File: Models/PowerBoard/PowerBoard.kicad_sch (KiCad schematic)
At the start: 0 parts

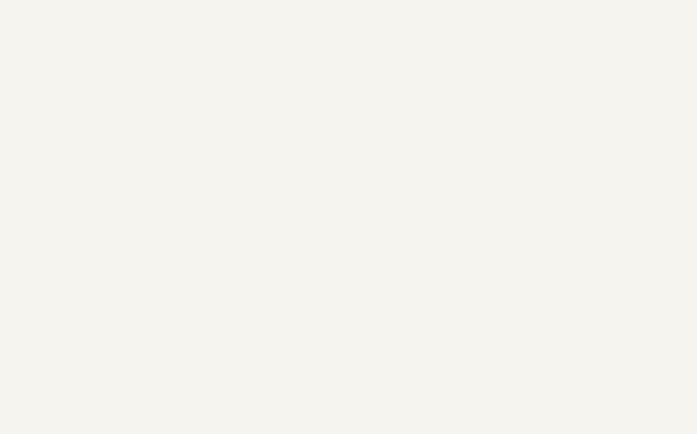
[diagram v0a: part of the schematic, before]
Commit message: Added mounting holes
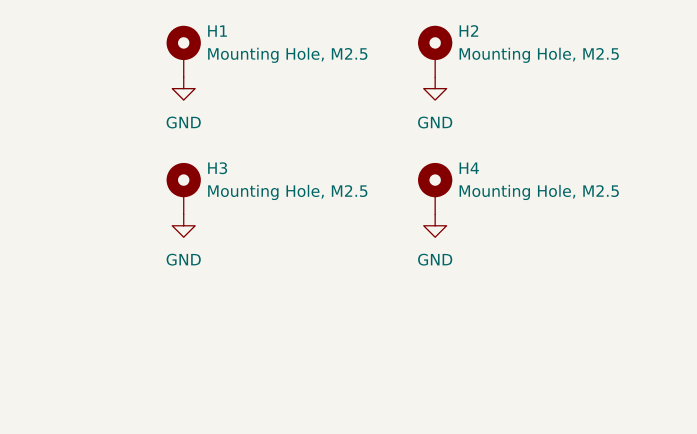
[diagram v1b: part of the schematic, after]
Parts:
- added H1, H2, H3, H4: Mounting Hole, M2.5, MountingHole:MountingHole_2.7mm_M2.5_DIN965_Pad, symbol Mechanical:MountingHole_Pad
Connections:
- new net GND: H1.1, H2.1, H3.1, H4.1

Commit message: Save progress
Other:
- note added: "15V: shielded -15V: shielded"
- note added: "18V: no external interface -18V: no external interface"
- note added: "5V (preamp): breadboard -5V (preamp): breadboard 2.5V: shielded -1.5V: shielded"
- note added: "5V: no external interface 3.3V: no external interface"
- note added: "interface to main board: many pin/socket connections external interface (shielded): (1) SMA (2) 1x4 pin socket, GND + OUT + OUT + GND external interface (breadboard): (1) 1x4 pin socket, GND + OUT + OUT + GND"
- note removed: "Allocate 2 pins on a large pin socket for each of the following nodes, in case design revisions require more boards: - 18V - -18V - GND - 5V (converter) - 3.3V - GND - 5V (preamp) - -5V (preamp)"

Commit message: Save progress
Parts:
- added J11, J14, J15, J5, J7, J9: Conn_01x04_Socket, symbol Connector:Conn_01x04_Socket
- added J12, J13, J4, J6: Conn_Coaxial, symbol Connector:Conn_Coaxial
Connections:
- net GND: now also J11.1 (Pin_1), J11.4 (Pin_4), J12.2 (Ext), J13.2 (Ext), J14.1 (Pin_1), J14.4 (Pin_4), J15.1 (Pin_1), J15.4 (Pin_4), J4.2 (Ext), J5.1 (Pin_1), J5.4 (Pin_4), J6.2 (Ext), J7.1 (Pin_1), J7.4 (Pin_4), J9.1 (Pin_1), J9.4 (Pin_4)
- new net: J14.2 (Pin_2), J14.3 (Pin_3)
- new net: J5.2 (Pin_2), J5.3 (Pin_3)
- new net: J11.2 (Pin_2), J11.3 (Pin_3)
- new net: J9.2 (Pin_2), J9.3 (Pin_3)
- new net: J7.2 (Pin_2), J7.3 (Pin_3)
- new net: J15.2 (Pin_2), J15.3 (Pin_3)
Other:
- moved on the sheet: H1, H2, H3, H4

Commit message: Save progress
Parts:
- added J8: Conn_01x09_Socket, symbol Connector:Conn_01x09_Socket
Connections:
- net -1.5V: now also J13.1 (In), J15.2 (Pin_2), J15.3 (Pin_3)
- net -15V: now also J6.1 (In), J7.2 (Pin_2), J7.3 (Pin_3), J8.4 (Pin_4)
- net 15V: now also J4.1 (In), J5.2 (Pin_2), J5.3 (Pin_3), J8.2 (Pin_2)
- net 2.5V: now also J12.1 (In), J14.2 (Pin_2), J14.3 (Pin_3)
- net 3.3V: now also J8.8 (Pin_8)
- net 5V: now also J8.6 (Pin_6)
- net GND: now also J8.1 (Pin_1), J8.3 (Pin_3), J8.5 (Pin_5), J8.7 (Pin_7), J8.9 (Pin_9)
- net -5V_PreAmp: now reaches J11.2 (Pin_2), J11.3 (Pin_3)
- net 5V_PreAmp: now reaches J9.2 (Pin_2), J9.3 (Pin_3)
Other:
- moved on the sheet: H1, H2, H3, H4

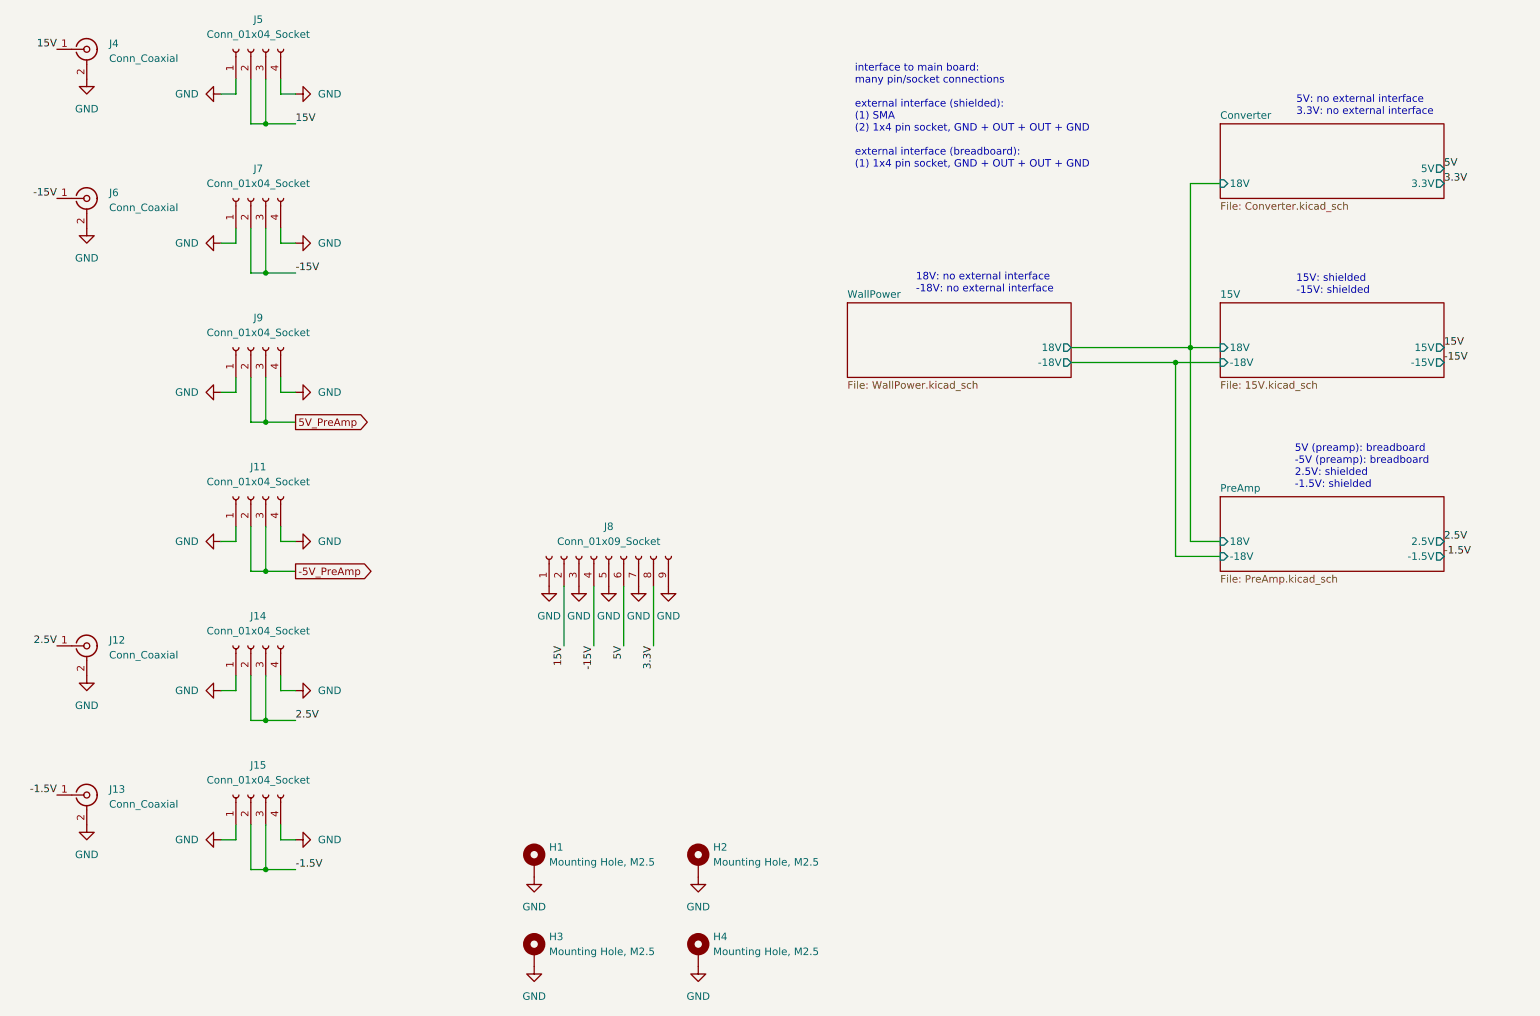
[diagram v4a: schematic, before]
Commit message: Connectors should be fully specified now
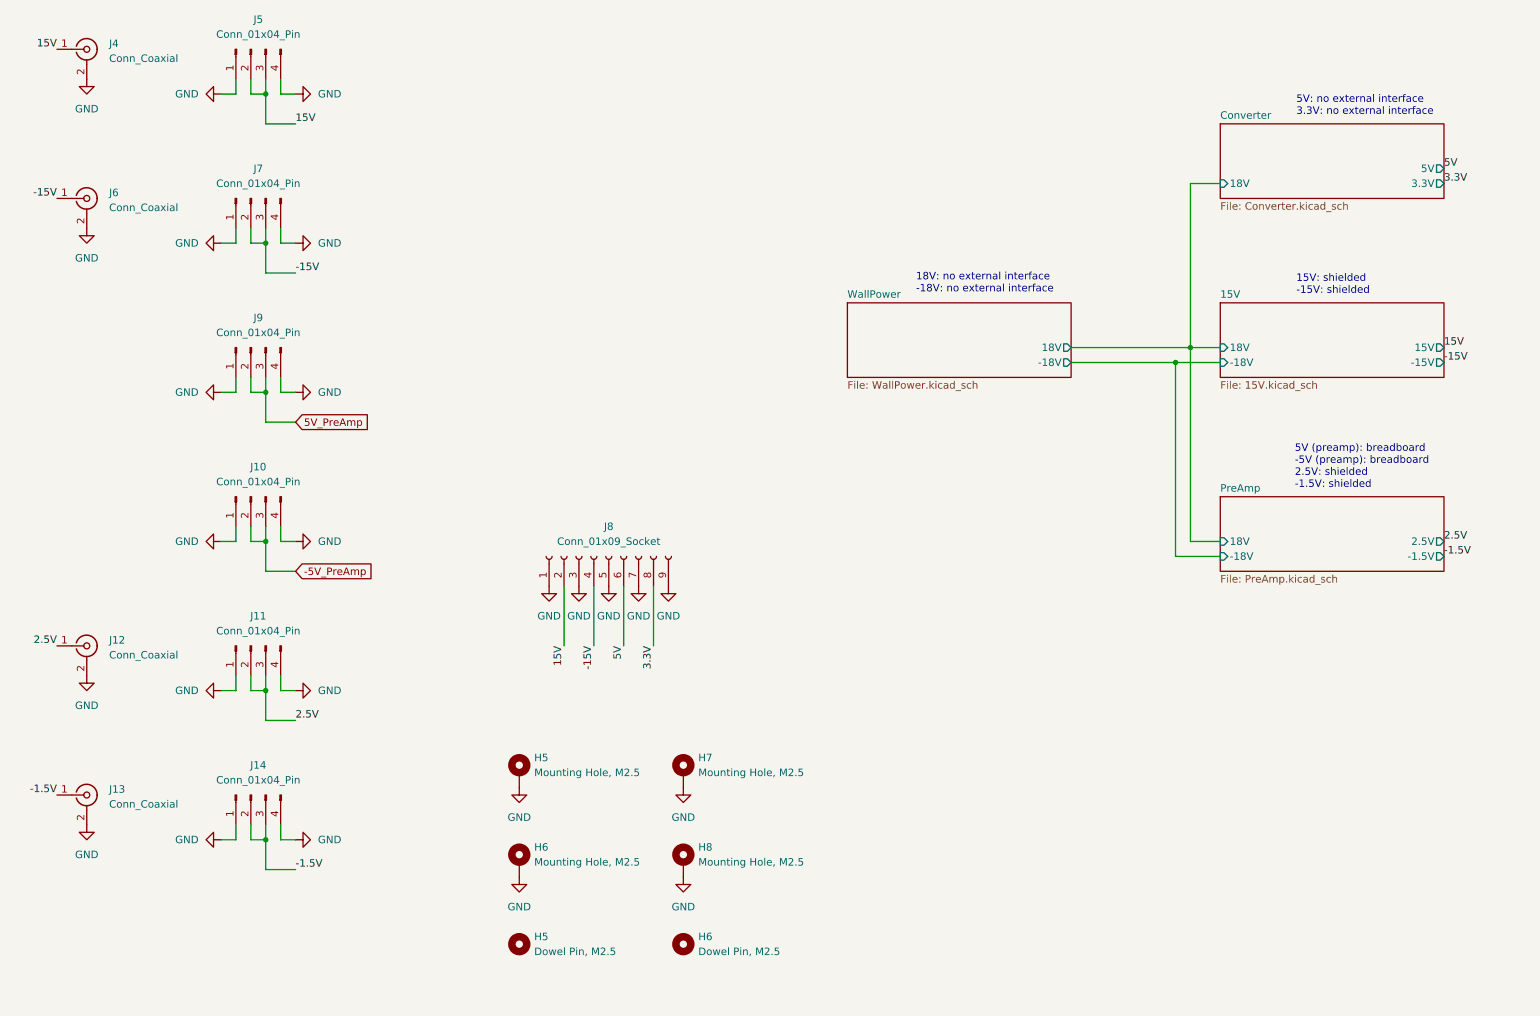
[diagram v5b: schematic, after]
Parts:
- removed H1, H2, H3, H4: Mounting Hole, M2.5, MountingHole:MountingHole_2.7mm_M2.5_DIN965_Pad, symbol Mechanical:MountingHole_Pad
- removed J11, J14, J15, J5, J7, J9: Conn_01x04_Socket, symbol Connector:Conn_01x04_Socket
- added H5, H6: Dowel Pin, M2.5, symbol Mechanical:MountingHole
- added H5, H6, H7, H8: Mounting Hole, M2.5, MountingHole:MountingHole_2.7mm_M2.5_DIN965_Pad, symbol Mechanical:MountingHole_Pad
- added J10, J11, J14, J5, J7, J9: Conn_01x04_Pin, symbol Connector:Conn_01x04_Pin
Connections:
- net -1.5V: now also J14.2 (Pin_2), J14.3 (Pin_3)
- net -15V: now also J7.2 (Pin_2), J7.3 (Pin_3)
- net -5V_PreAmp: now also J10.2 (Pin_2), J10.3 (Pin_3)
- net 15V: now also J5.2 (Pin_2), J5.3 (Pin_3)
- net 2.5V: now also J11.2 (Pin_2), J11.3 (Pin_3)
- net 5V_PreAmp: now also J9.2 (Pin_2), J9.3 (Pin_3)
- net GND: now also H5.1, H6.1, H7.1, H8.1, J10.1 (Pin_1), J10.4 (Pin_4), J11.1 (Pin_1), J11.4 (Pin_4), J14.1 (Pin_1), J14.4 (Pin_4), J5.1 (Pin_1), J5.4 (Pin_4), J7.1 (Pin_1), J7.4 (Pin_4), J9.1 (Pin_1), J9.4 (Pin_4)
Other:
- note removed: "interface to main board: many pin/socket connections external interface (shielded): (1) SMA (2) 1x4 pin socket, GND + OUT + OUT + GND external interface (breadboard): (1) 1x4 pin socket, GND + OUT + OUT + GND"

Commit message: Passes ERC
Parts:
- renumbered H5 to H1, H6 to H2, H5 to H3, H7 to H4, H8 to H5, J4 to J1, J14 to J10, J8 to J11, J6 to J2, J12 to J3, J13 to J4, J7 to J6, J9 to J7, J10 to J8, J11 to J9

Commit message: Assigned footprints
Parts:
- H1, H2, H4, H5: footprint MountingHole:MountingHole_2.7mm_M2.5_DIN965_Pad -> Connector_Custom:Keystone_24929
- H3, H6: footprint (none) -> Connector_Custom:DowelPin_2.5mm
- J1, J2, J3, J4: footprint (none) -> Connector_Custom:RFPC-SMA27-F
- J10, J5, J6, J7, J8, J9: footprint (none) -> Connector_Custom:PinConnector_1x4
- J11: footprint (none) -> Connector_Custom:PinConnector_1x9
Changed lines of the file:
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@@
 			)
 		)
-		(property "Footprint" ""
+		(property "Footprint" "Connector_Custom:RFPC-SMA27-F"
 			(at 38.1 50.8 0)
 			(effects
@@
 			)
 		)
-		(property "Footprint" ""
+		(property "Footprint" "Connector_Custom:DowelPin_2.5mm"
 			(at 139.7 177.8 0)
 			(effects
@@
 			)
 		)
-		(property "Footprint" ""
+		(property "Footprint" "Connector_Custom:PinConnector_1x4"
 			(at 66.04 152.4 0)
 			(effects
@@
 			)
 		)
-		(property "Footprint" ""
+		(property "Footprint" "Connector_Custom:DowelPin_2.5mm"
 			(at 111.76 177.8 0)
 			(effects
@@
 			)
 		)
-		(property "Footprint" ""
+		(property "Footprint" "Connector_Custom:RFPC-SMA27-F"
 			(at 38.1 127 0)
 			(effects
@@
 			)
 		)
-		(property "Footprint" "MountingHole:MountingHole_2.7mm_M2.5_DIN965_Pad"
+		(property "Footprint" "Connector_Custom:Keystone_24929"
 			(at 139.7 163.83 0)
 			(effects
@@
 			)
 		)
-		(property "Footprint" ""
+		(property "Footprint" "Connector_Custom:PinConnector_1x9"
 			(at 127 111.76 0)
 			(effects
@@
 			)
 		)
-		(property "Footprint" "MountingHole:MountingHole_2.7mm_M2.5_DIN965_Pad"
+		(property "Footprint" "Connector_Custom:Keystone_24929"
 			(at 139.7 148.59 0)
 			(effects
@@
 			)
 		)
-		(property "Footprint" ""
+		(property "Footprint" "Connector_Custom:PinConnector_1x4"
 			(at 66.04 25.4 0)
 			(effects
@@
 			)
 		)
-		(property "Footprint" "MountingHole:MountingHole_2.7mm_M2.5_DIN965_Pad"
+		(property "Footprint" "Connector_Custom:Keystone_24929"
 			(at 111.76 148.59 0)
 			(effects
@@
 			)
 		)
-		(property "Footprint" ""
+		(property "Footprint" "Connector_Custom:RFPC-SMA27-F"
 			(at 38.1 25.4 0)
 			(effects
@@
 			)
 		)
-		(property "Footprint" ""
+		(property "Footprint" "Connector_Custom:PinConnector_1x4"
 			(at 66.04 127 0)
 			(effects
@@
 			)
 		)
-		(property "Footprint" ""
+		(property "Footprint" "Connector_Custom:PinConnector_1x4"
 			(at 66.04 76.2 0)
 			(effects
@@
 			)
 		)
-		(property "Footprint" ""
+		(property "Footprint" "Connector_Custom:RFPC-SMA27-F"
 			(at 38.1 152.4 0)
 			(effects
@@
 			)
 		)
-		(property "Footprint" ""
+		(property "Footprint" "Connector_Custom:PinConnector_1x4"
 			(at 66.04 101.6 0)
 			(effects
@@
 			)
 		)
-		(property "Footprint" "MountingHole:MountingHole_2.7mm_M2.5_DIN965_Pad"
+		(property "Footprint" "Connector_Custom:Keystone_24929"
 			(at 111.76 163.83 0)
 			(effects
@@
 			)
 		)
-		(property "Footprint" ""
+		(property "Footprint" "Connector_Custom:PinConnector_1x4"
 			(at 66.04 50.8 0)
 			(effects

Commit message: Save progress
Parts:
- J1, J2, J3, J4: footprint Connector_Custom:RFPC-SMA27-F -> (none); Cost $1.916 -> $3.146; Purchase Link https://www.digikey.com/en/products/detail/gct/RFPC-SMA27-F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 -> https://www.digikey.com/en/products/detail/molex/0733660030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
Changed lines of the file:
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@@
 			)
 		)
-		(property "Footprint" "Connector_Custom:RFPC-SMA27-F"
+		(property "Footprint" ""
 			(at 38.1 50.8 0)
 			(effects
@@
 			)
 		)
-		(property "Purchase Link" "https://www.digikey.com/en/products/detail/gct/RFPC-SMA27-F/22162144"
+		(property "Purchase Link" "https://www.digikey.com/en/products/detail/molex/0733660030/1465162"
 			(at 38.1 50.8 0)
 			(effects
@@
 			)
 		)
-		(property "Cost" "$1.916"
+		(property "Cost" "$3.146"
 			(at 38.1 50.8 0)
 			(effects
@@
 			)
 		)
-		(property "Footprint" "Connector_Custom:RFPC-SMA27-F"
+		(property "Footprint" ""
 			(at 38.1 127 0)
 			(effects
@@
 			)
 		)
-		(property "Purchase Link" "https://www.digikey.com/en/products/detail/gct/RFPC-SMA27-F/22162144"
+		(property "Purchase Link" "https://www.digikey.com/en/products/detail/molex/0733660030/1465162"
 			(at 38.1 127 0)
 			(effects
@@
 			)
 		)
-		(property "Cost" "$1.916"
+		(property "Cost" "$3.146"
 			(at 38.1 127 0)
 			(effects
@@
 			)
 		)
-		(property "Footprint" "Connector_Custom:RFPC-SMA27-F"
+		(property "Footprint" ""
 			(at 38.1 25.4 0)
 			(effects
@@
 			)
 		)
-		(property "Purchase Link" "https://www.digikey.com/en/products/detail/gct/RFPC-SMA27-F/22162144"
+		(property "Purchase Link" "https://www.digikey.com/en/products/detail/molex/0733660030/1465162"
 			(at 38.1 25.4 0)
 			(effects
@@
 			)
 		)
-		(property "Cost" "$1.916"
+		(property "Cost" "$3.146"
 			(at 38.1 25.4 0)
 			(effects
@@
 			)
 		)
-		(property "Footprint" "Connector_Custom:RFPC-SMA27-F"
+		(property "Footprint" ""
 			(at 38.1 152.4 0)
 			(effects
@@
 			)
 		)
-		(property "Purchase Link" "https://www.digikey.com/en/products/detail/gct/RFPC-SMA27-F/22162144"
+		(property "Purchase Link" "https://www.digikey.com/en/products/detail/molex/0733660030/1465162"
 			(at 38.1 152.4 0)
 			(effects
@@
 			)
 		)
-		(property "Cost" "$1.916"
+		(property "Cost" "$3.146"
 			(at 38.1 152.4 0)
 			(effects
